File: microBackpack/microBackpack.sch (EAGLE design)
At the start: 0 parts

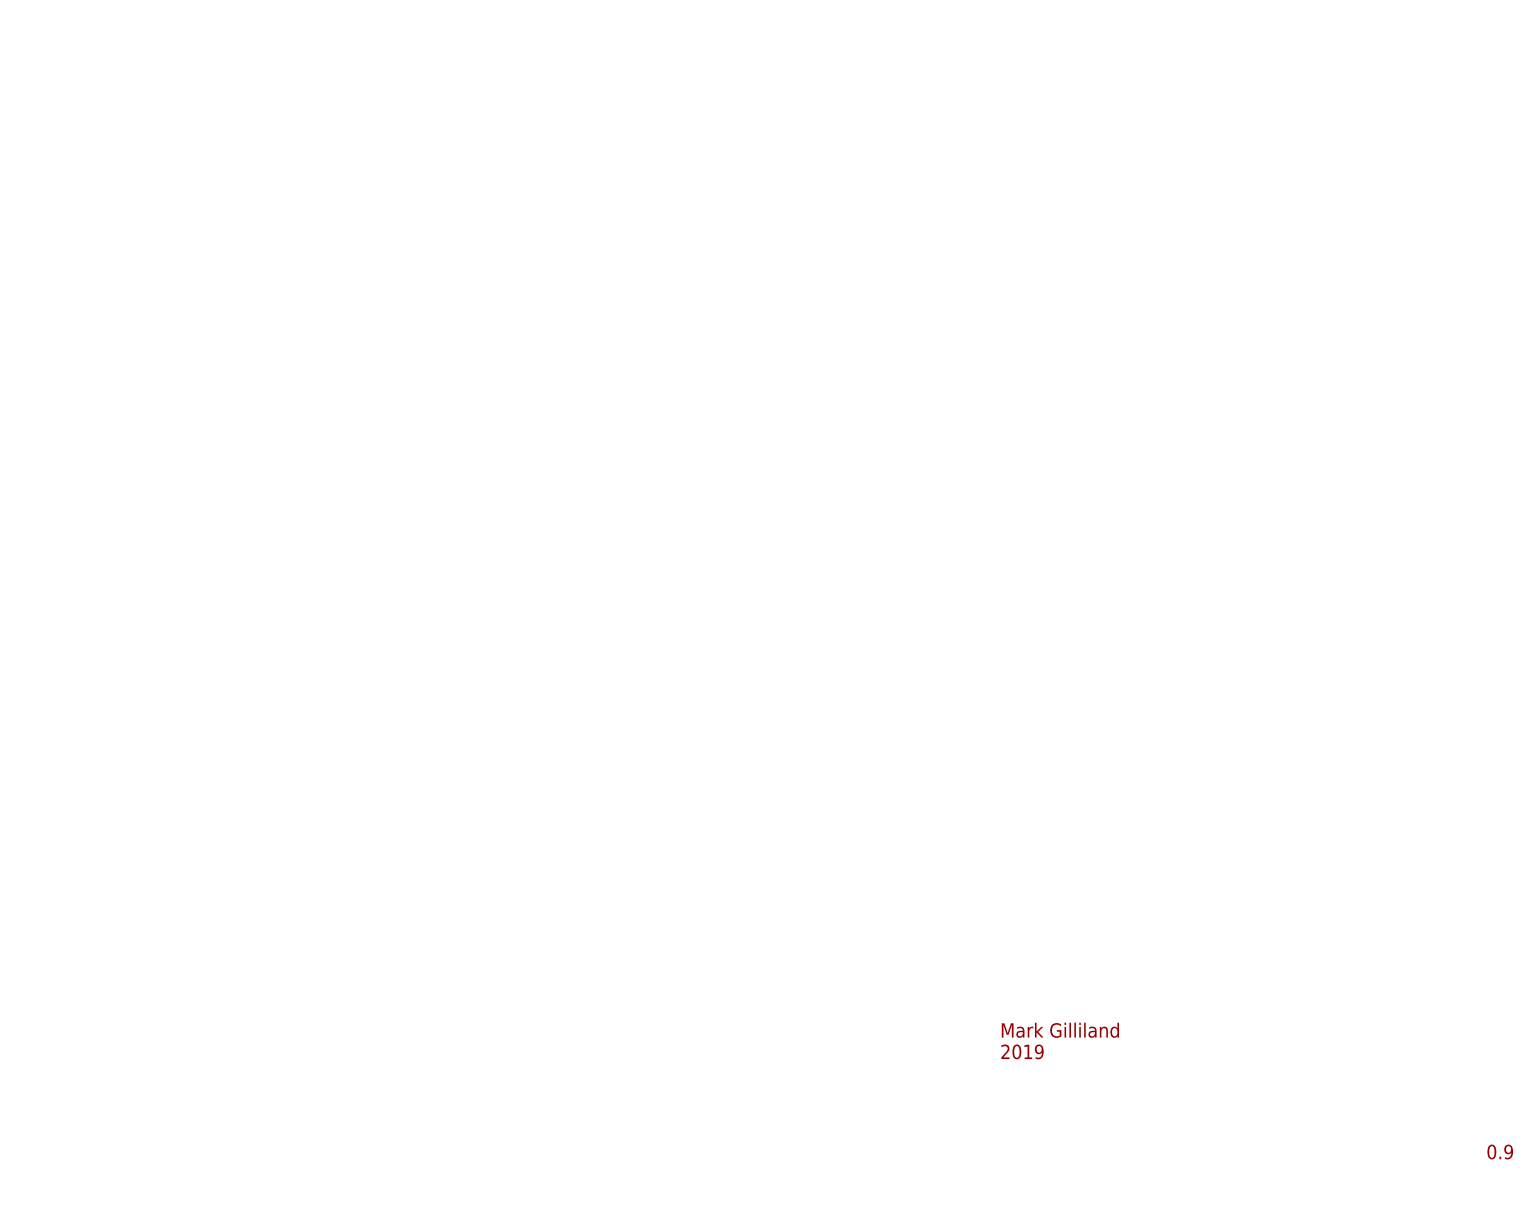
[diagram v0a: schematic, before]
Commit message: Added components to library and schem
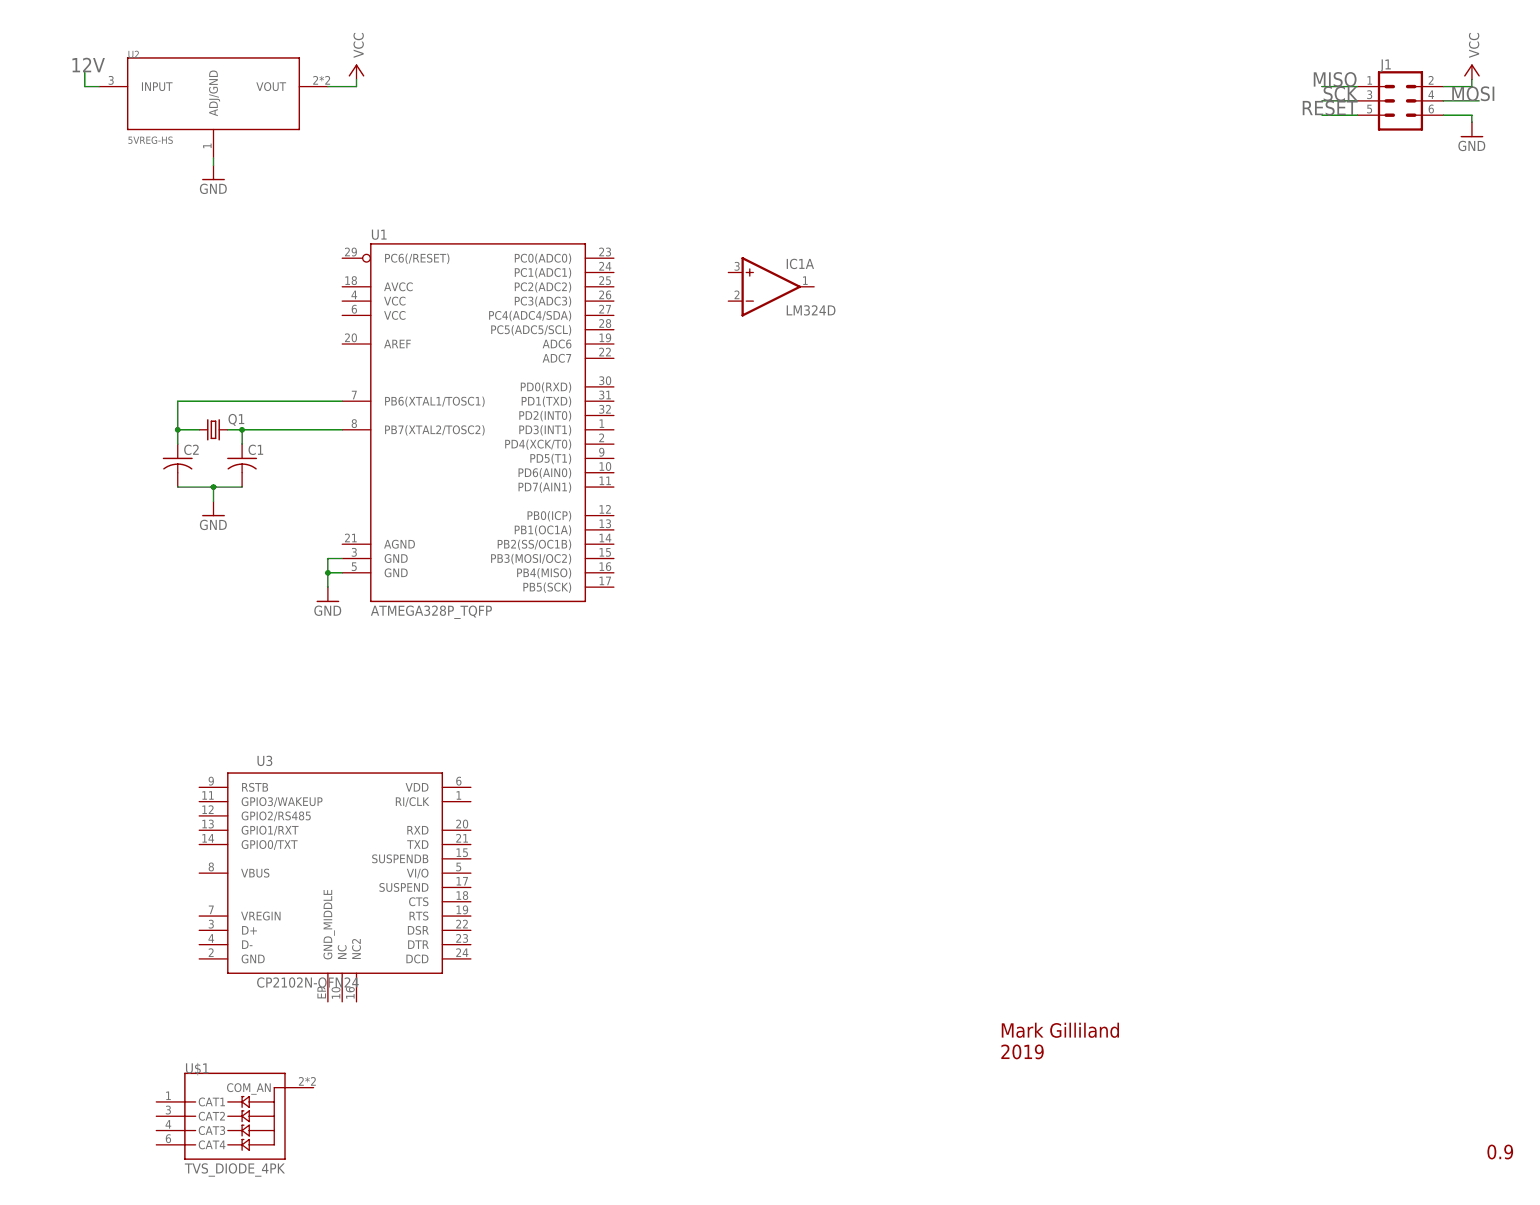
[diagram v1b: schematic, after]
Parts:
- added C1, C2: (no value), rcl:C-USC0805
- added IC1: LM324D, linear:LM324D
- added J1: (no value), SparkFun-Connectors:CONN_03X22X3_SILK_MALE_PTH
- added Q1: (no value), crystal:CRYSTALHC49U70
- added U$1: TVS_DIODE_4PK, microBackpackLib:TVS_DIODE_4PK
- added U1: ATMEGA328P_TQFP, SparkFun-IC-Microcontroller:ATMEGA328P_TQFP
- added U2: 5VREG-HS, microBackpackLib:5VREG-HS
- added U3: CP2102N-QFN24, microBackpackLib:CP2102N-QFN24
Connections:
- new net 12V: U2.INPUT
- new net GND: C1.2, C2.2, J1.6, U1.GND@3, U1.GND@5, U2.ADJ/GND
- new net MISO: J1.1
- new net MOSI: J1.4
- new net N$1: C1.1, Q1.2, U1.PB7(XTAL2/TOSC2)
- new net N$2: C2.1, Q1.1, U1.PB6(XTAL1/TOSC1)
- new net RESET: J1.5
- new net SCK: J1.3
- new net VCC: J1.2, U2.VOUT

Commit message: Added more components
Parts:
- removed IC1: LM324D, linear:LM324D
- added C3: 1uF, rcl:C-USC0805
- added C6: 10nF, rcl:C-USC0805
- added IC2: LM324D, linear:LM324D
- added J2: USB_B_PTH, SparkFun-Connectors:USB_B_PTH
- added J3: (no value), SparkFun-Connectors:CONN_04X2
- added J4: 2X6 FEMALE, SparkFun-Connectors:CONN_06X2PTH_FEMALE
- added J5: (no value), SparkFun-Connectors:CONN_06SILK_FEMALE_PTH
- added R1, R2: 1k, rcl:R-US_R0805
- added S1: MOMENTARY-SWITCH-SPST-SMD-5.2-REDUNDANT, SparkFun-Switches:MOMENTARY-SWITCH-SPST-SMD-5.2-REDUNDANT
- added U$2: LM4040-V-REF, microBackpackLib:LM4040-V-REF
- added U4: TVS_DIODE_4PK, microBackpackLib:TVS_DIODE_4PK
- added U5: MCP4728, microBackpackLib:MCP4728
- C1, C2: value (none) -> 22pF
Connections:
- new net A2: J3.5
- new net A3: J3.7
- new net AD0+: J3.1
- new net AD0-: J3.2
- new net AD1+: J3.3
- new net AD1-: J3.4
- new net ADC0: U1.PC0(ADC0)
- new net ADC1: U1.PC1(ADC1)
- new net ADC2: U1.PC2(ADC2)
- new net ADC3: U1.PC3(ADC3)
- new net ADC6: U1.ADC6
- new net ADC7: U1.ADC7
- new net DIO0: J4.1, U1.PD2(INT0)
- new net DIO1: J4.2, U1.PD3(INT1)
- new net DIO2: J4.3, U1.PD4(XCK/T0)
- new net DIO3: J4.4, U1.PD5(T1)
- new net DIO4: J4.5, U1.PD6(AIN0)
- new net DIO5: J4.6, U1.PD7(AIN1)
- new net DIO6: J4.7, U1.PB0(ICP)
- new net DIO7: J4.8, U1.PB1(OC1A)
- new net I_OUT: J5.5
- new net I_SET: J5.3
- new net LDAC: U1.PB2(SS/OC1B), U5.LDAC-
- new net MCU2USB: U1.PD1(TXD)
- new net N$3: R1.1, U$2.+IN, U1.AREF
- new net N$4: J2.GND, J2.SHIELD, U$1.COM_AN, U3.GND
- new net N$5: J2.VBUS, U3.VBUS
- new net N$7: J2.D-, U3.D-
- new net N$8: J2.D+, U3.D+
- new net SCL: U1.PC5(ADC5/SCL), U5.SCL
- new net SDA: U1.PC4(ADC4/SDA), U5.SDA
- new net USB2MCU: U1.PD0(RXD)
- new net V_OUT: J5.4
- new net V_SET: J5.2
- net 12V: now also J5.1
- net GND: now also C3.2, C6.2, J3.6, J3.8, J4.12, J5.6, S1.1, U$2.-IN, U1.AGND, U5.VSS
- net MISO: now also U1.PB4(MISO)
- net MOSI: now also U1.PB3(MOSI/OC2)
- net RESET: now also R2.1, S1.2, U1.PC6(/RESET)
- net SCK: now also U1.PB5(SCK)
- net VCC: now also C3.1, C6.1, R1.2, R2.2, U1.AVCC, U1.VCC@4, U1.VCC@6, U5.VDD

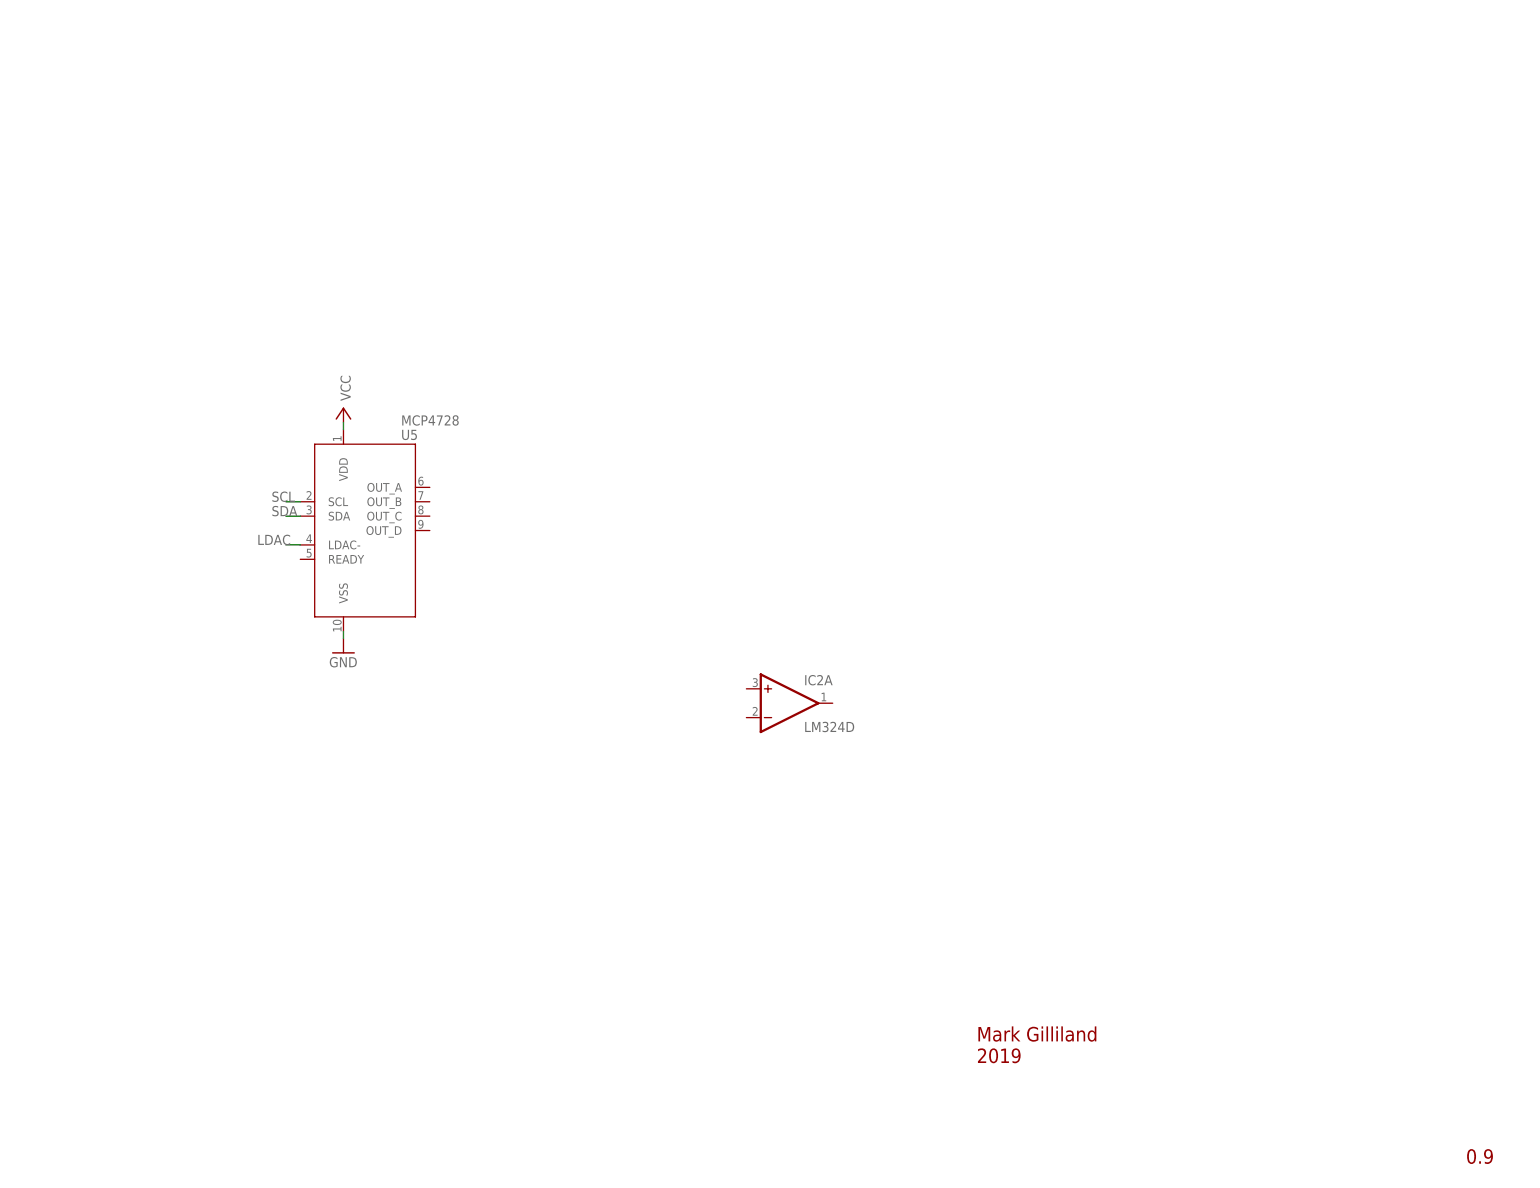
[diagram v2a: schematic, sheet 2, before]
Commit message: Added analog circuitry. Most of schem is done. Still must do optoisolation and DIO protection
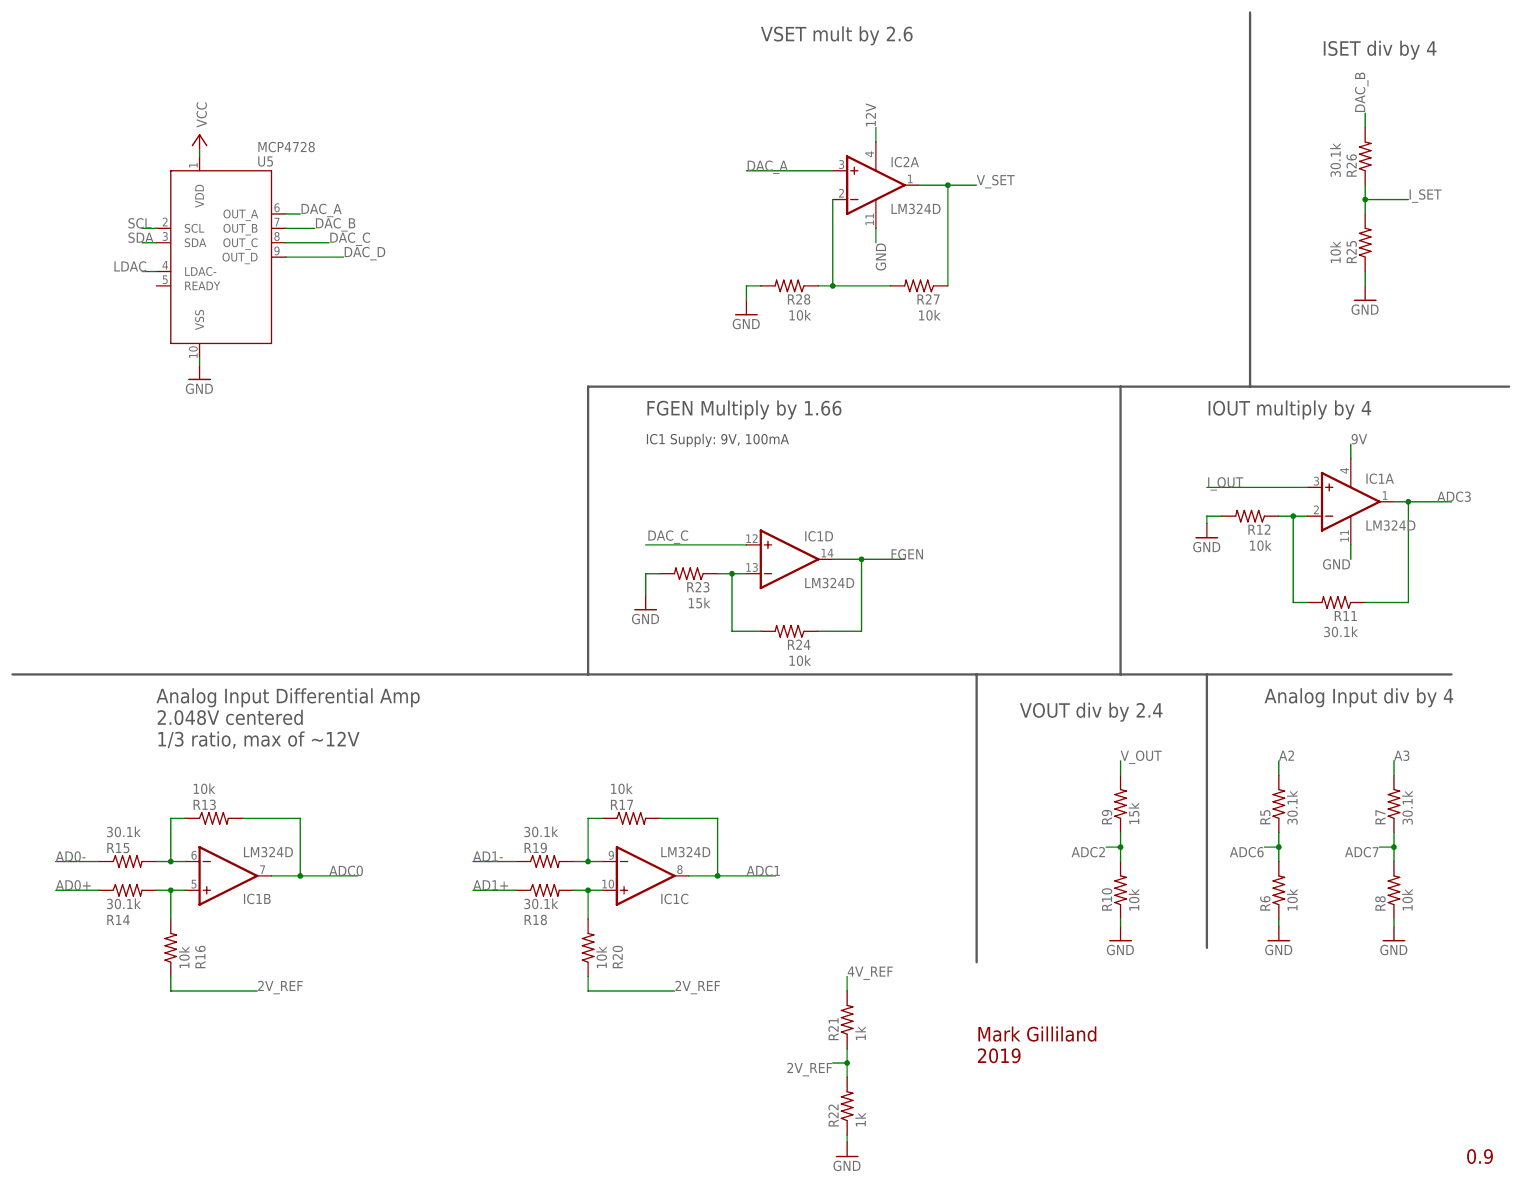
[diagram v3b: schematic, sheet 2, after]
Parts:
- added C4, C8: 10nF, rcl:C-USC0805
- added C5, C7, C9: 1uF, rcl:C-USC0805
- added IC1: LM324D, linear:LM324D
- added R10, R12, R13, R16, R17, R20, R24, R25, R27, R28, R6, R8: 10k, rcl:R-US_R0805
- added R11, R14, R15, R18, R19, R26, R5, R7: 30.1k, rcl:R-US_R0805
- added R21, R22: 1k, rcl:R-US_R0805
- added R23, R9: 15k, rcl:R-US_R0805
- added R3, R4: 4.7k, rcl:R-US_R0805
- added U6: 78L09F, linear:78L09F
- renumbered U$2 to D1
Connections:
- new net 2V_REF: R16.1, R20.1, R21.1, R22.2
- new net 4V_REF: C8.1, D1.+IN, R1.1, R21.2, U1.AREF
- new net 9V: C4.1, C5.1, IC1P.V+, U6.VO
- new net DAC_A: IC2A.+IN, U5.OUT_A
- new net DAC_B: R26.2, U5.OUT_B
- new net DAC_C: IC1D.+IN, U5.OUT_C
- new net DAC_D: U5.OUT_D
- new net FGEN: IC1D.OUT, R24.1
- new net N$10: IC1B.+IN, R14.2, R16.2
- new net N$11: IC2A.-IN, R27.2, R28.1
- new net N$14: IC1C.-IN, R17.1, R19.2
- new net N$15: IC1C.+IN, R18.2, R20.2
- new net N$6: IC1A.-IN, R11.2, R12.1
- new net N$9: IC1B.-IN, R13.1, R15.2
- net 12V: now also C7.1, C9.1, IC2P.V+, U6.VI
- net A2: now also R5.2
- net A3: now also R7.2
- net AD0+: now also R14.1
- net AD0-: now also R15.1
- net AD1+: now also R18.1
- net AD1-: now also R19.1
- net ADC0: now also IC1B.OUT, R13.2
- net ADC1: now also IC1C.OUT, R17.2
- net ADC2: now also R10.2, R9.1
- net ADC3: now also IC1A.OUT, R11.1
- net ADC6: now also R5.1, R6.2
- net ADC7: now also R7.1, R8.2
- net GND: now also C4.2, C5.2, C7.2, C8.2, C9.2, IC1P.V-, IC2P.V-, R10.1, R12.2, R22.1, R23.2, R25.1, R28.2, R6.1, R8.1, U6.GND, U6.GND@1
- net I_OUT: now also IC1A.+IN
- net I_SET: now also R25.2, R26.1
- net N$3: now also IC1D.-IN, R23.1, R24.2; no longer D1.+IN, R1.1, U1.AREF
- net SCL: now also R4.1
- net SDA: now also R3.1
- net VCC: now also R3.2, R4.2
- net V_OUT: now also R9.2
- net V_SET: now also IC2A.OUT, R27.1
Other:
- note added: "Analog Input Differential Amp 2.048V centered 1/3 ratio, max of ~12V"
- note added: "Analog Input div by 4"
- note added: "FGEN Multiply by 1.66"
- note added: "IC1 Supply: 9V, 100mA"
- note added: "IOUT multiply by 4"
- note added: "ISET div by 4"
- note added: "VOUT div by 2.4"
- note added: "VSET mult by 2.6"
- moved on the sheet: IC2A, U5
